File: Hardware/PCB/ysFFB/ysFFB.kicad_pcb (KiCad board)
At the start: 2 copper layers, 423.6 x 175 mm, 279 parts, among them J1 Synth_power_2x5, J10 AudioJack2, J11 AudioJack2, J12 AudioJack2, J13 AudioJack2, J14 AudioJack2, J15 Conn_01x04, J16 Conn_01x03, J2 Conn_01x08, J3 Conn_01x06, J4 Conn_01x04, J5 Conn_02x07_Odd_Even, J6 Conn_01x03, J7 Conn_01x08, J8 Conn_02x07_Odd_Even, J9 Conn_01x06, U1 TL074, U2 TL074, U3 TL074, U4 TL074, U5 TL074, U6 TL074, U7 TL074, U8 TL074

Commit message: Fix socket that looked suspiciously like a header. Fix every last remaining inconsistency.
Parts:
- J8: footprint Connector_PinHeader_2.54mm:PinHeader_2x07_P2.54mm_Vertical -> Connector_PinSocket_2.54mm:PinSocket_2x07_P2.54mm_Vertical
- moved J8 2.54 mm to (-28.8, 183.9)
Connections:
- J15 pad 2: ALL_P -> ODD_P
- J15 pad 3: ODD_P -> EVEN_P
- J15 pad 4: EVEN_P -> ALL_P
- J7 pad 1: /Panel components/BP8PP -> /Panel components/BP7PP
- J7 pad 2: /Panel components/BP6PP -> /Panel components/BP5PP
- J7 pad 3: /Panel components/BP4PP -> /Panel components/BP3PP
- J7 pad 4: /Panel components/BP2PP -> /Panel components/BP1PP
- J7 pad 5: /Panel components/BP1PP -> /Panel components/BP2PP
- J7 pad 6: /Panel components/BP3PP -> /Panel components/BP4PP
- J7 pad 7: /Panel components/BP5PP -> /Panel components/BP6PP
- J7 pad 8: /Panel components/BP7PP -> /Panel components/BP8PP
- J9 pad 1: /Panel components/HPPP -> /Panel components/LPP
- J9 pad 2: /Panel components/BP12P -> /Panel components/BP11PP
- J9 pad 3: /Panel components/BP10PP -> /Panel components/BP9PP
- J9 pad 4: /Panel components/BP9PP -> /Panel components/BP10PP
- J9 pad 5: /Panel components/BP11PP -> /Panel components/BP12P
- J9 pad 6: /Panel components/LPP -> /Panel components/HPPP
- RV1 pad 3: /Panel components/BP8PP -> /Panel components/BP7PP
- RV10 pad 3: /Panel components/BP12P -> /Panel components/BP11PP
- RV11 pad 3: /Panel components/BP10PP -> /Panel components/BP9PP
- RV12 pad 3: /Panel components/BP9PP -> /Panel components/BP10PP
- RV13 pad 3: /Panel components/BP11PP -> /Panel components/BP12P
- RV14 pad 3: /Panel components/LPP -> /Panel components/HPPP
- RV2 pad 3: /Panel components/BP6PP -> /Panel components/BP5PP
- RV3 pad 3: /Panel components/BP4PP -> /Panel components/BP3PP
- RV4 pad 3: /Panel components/BP2PP -> /Panel components/BP1PP
- RV5 pad 3: /Panel components/BP1PP -> /Panel components/BP2PP
- RV6 pad 3: /Panel components/BP3PP -> /Panel components/BP4PP
- RV7 pad 3: /Panel components/BP5PP -> /Panel components/BP6PP
- RV8 pad 3: /Panel components/BP7PP -> /Panel components/BP8PP
- RV9 pad 3: /Panel components/HPPP -> /Panel components/LPP
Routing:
- net /Panel components/LPP: track 111.0 -> 260.8 mm
- net /Panel components/HPPP: track 260.8 -> 111.0 mm
- net P2_12: track 235.1 -> 175.7 mm
- net P2_H: track 183.4 -> 242.6 mm
- net P2_11: track 154.3 -> 210.9 mm
- net P2_10: track 201.7 -> 146.6 mm
- net P2_8: track 171.8 -> 117.5 mm
- net P2_9: track 125.3 -> 179.3 mm
- net P2_7: track 96.2 -> 147.6 mm
- net P2_5: track 67.2 -> 115.9 mm
- net P2_3: track 38.1 -> 84.2 mm
- net P2_6: track 132.4 -> 88.5 mm
- net P2_4: track 100.6 -> 60.2 mm
- net P2_2: track 61.8 -> 30.8 mm
- net /Panel components/BP9PP: track 120.6 -> 134.7 mm
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
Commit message: submodules
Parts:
- removed G***: LOGO, ysFFB:ysFFB-aux-slide2_holes
- added GRAF1: Holes, ysFFB:ysFFB-aux-slide2_holes, F.Cu at (-104.2, 121.0)
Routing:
- net +12V: track 401.6 -> 402.8 mm

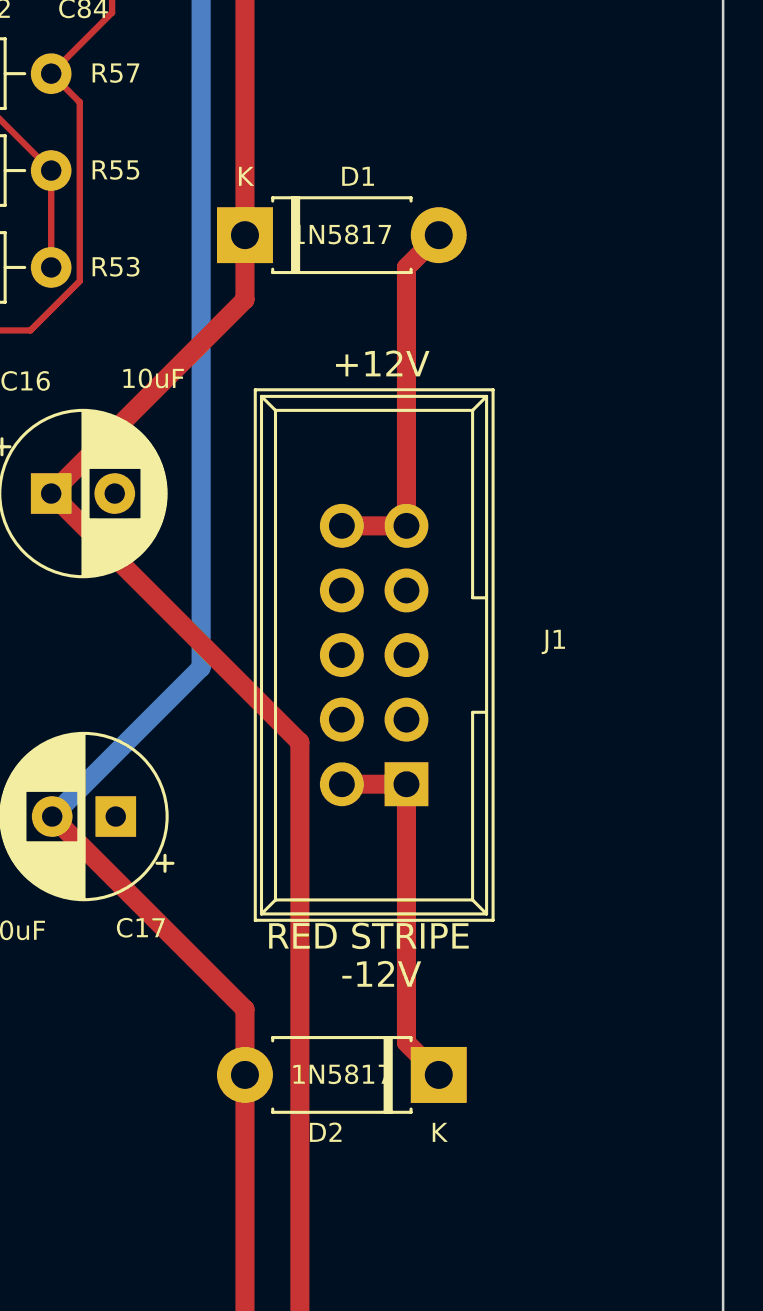
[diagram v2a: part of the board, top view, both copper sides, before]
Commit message: Clean up libraries, Schottky footprint update
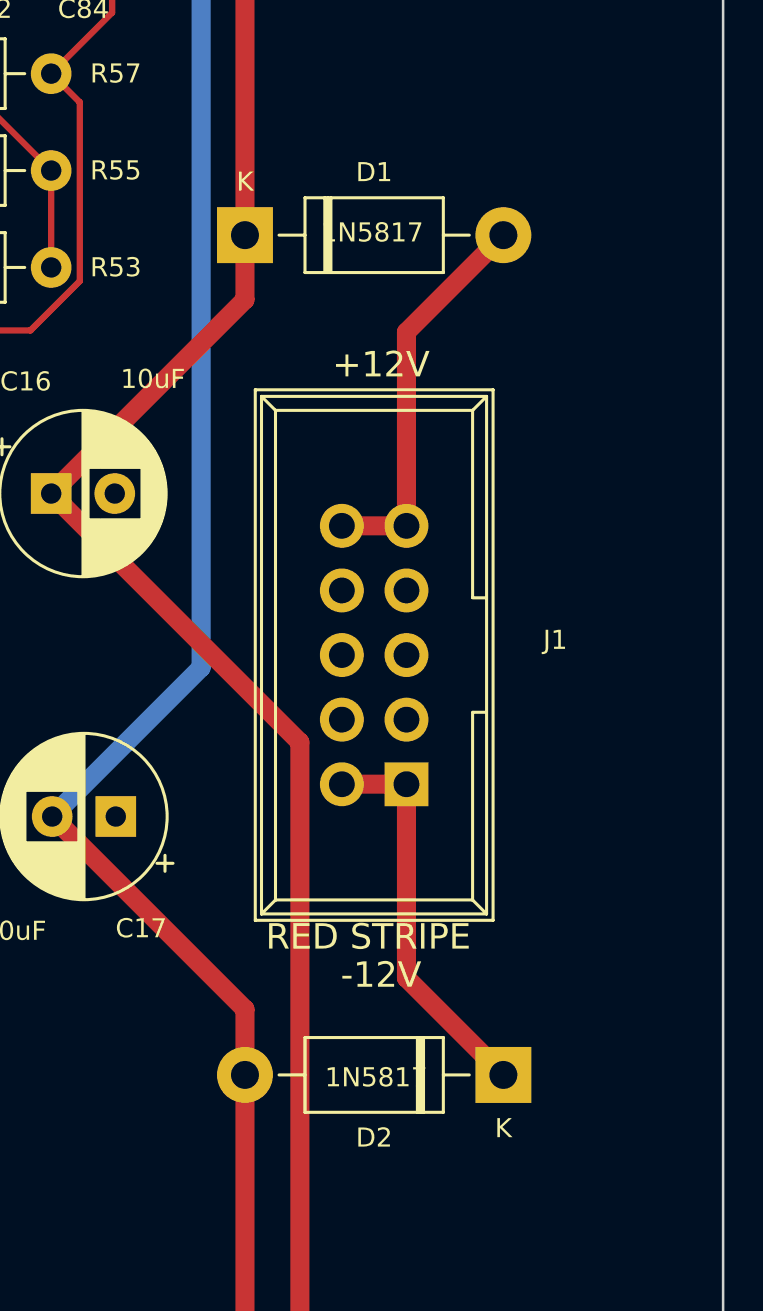
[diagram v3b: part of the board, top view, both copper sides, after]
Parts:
- D1, D2: footprint ao_tht:D_DO-41_SOD81_P7.62mm_Horizontal -> ao_tht:D_DO-41_SOD81_P10.16mm_Horizontal
- moved D2 2.54 mm to (213.8, 133.1)
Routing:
- net /+12_IN: track 14.5 -> 15.5 mm
- net /-12_IN: track 14.5 -> 15.5 mm

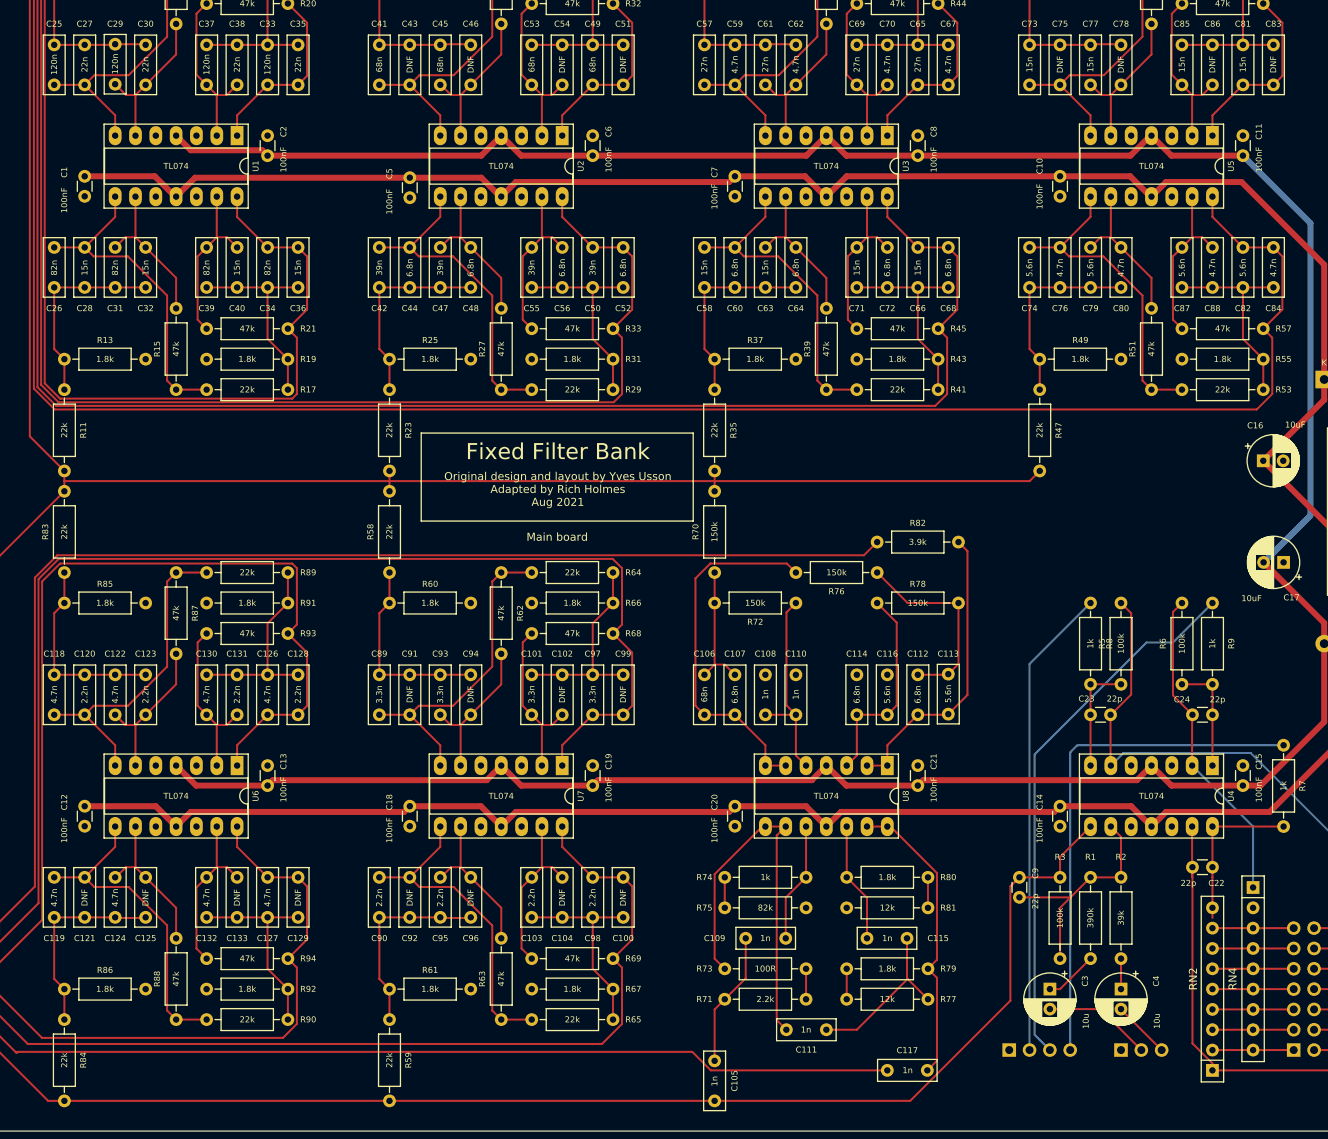
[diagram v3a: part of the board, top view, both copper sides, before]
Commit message: Cap vals on PCB, revised panel
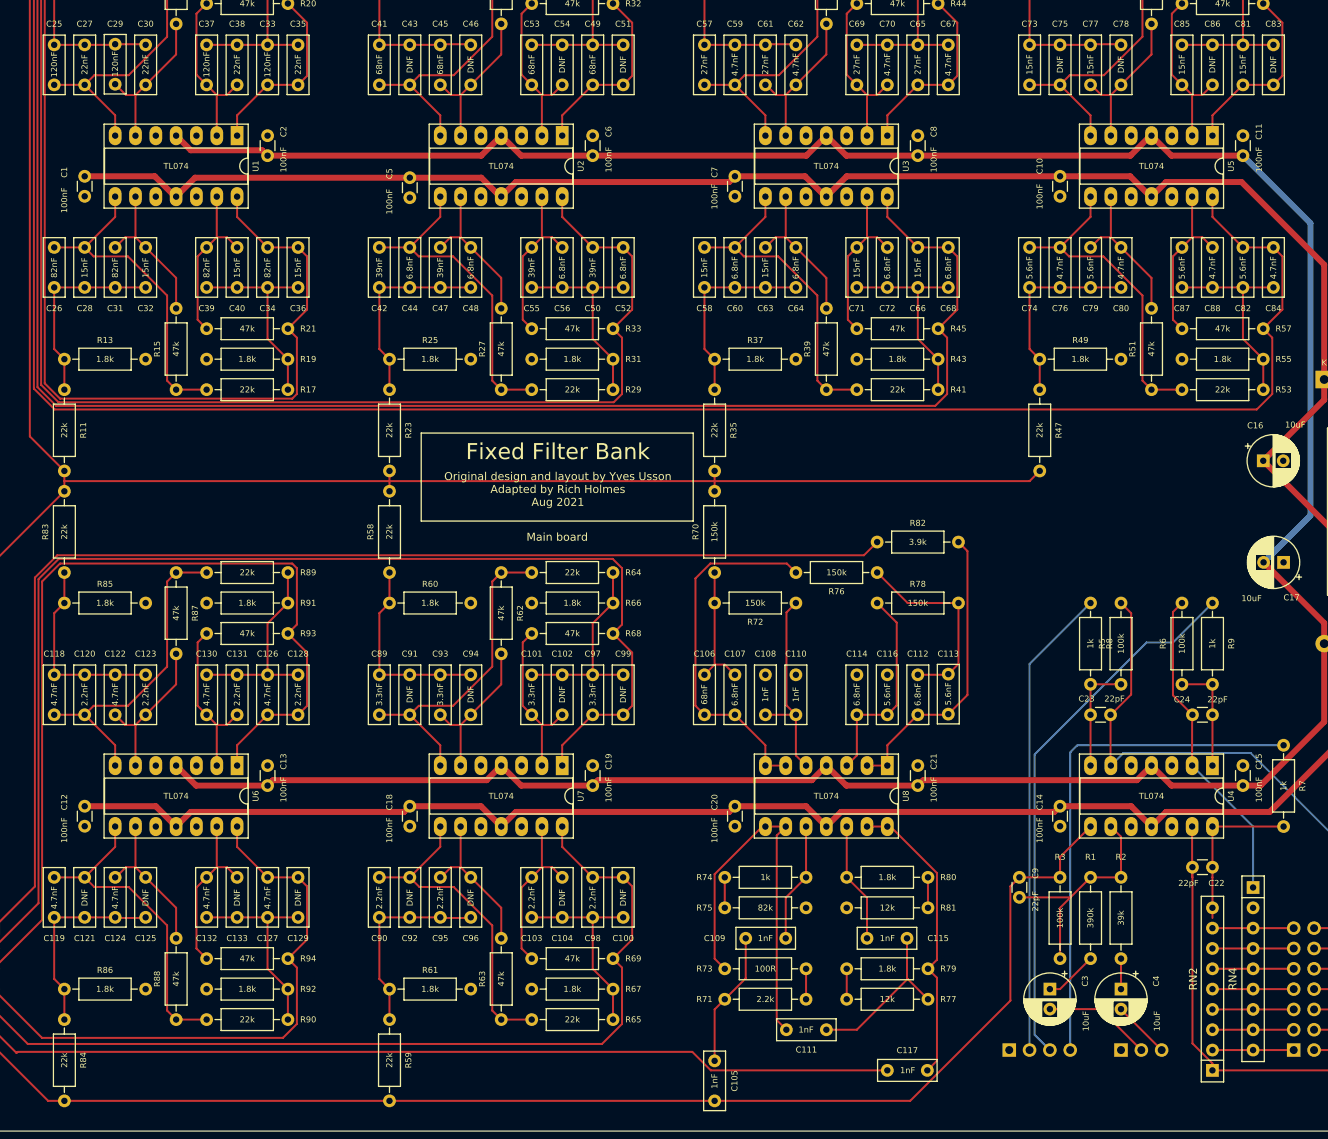
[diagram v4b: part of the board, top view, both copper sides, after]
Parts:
- C101, C89, C93, C97: value 3.3n -> 3.3nF
- C103, C120, C123, C128, C131, C90, C95, C98: value 2.2n -> 2.2nF
- C105, C108, C109, C110, C111, C115, C117: value 1n -> 1nF
- C106, C41, C45, C49, C53: value 68n -> 68nF
- C107, C112, C114, C44, C48, C52, C56, C60, C64, C68, C72: value 6.8n -> 6.8nF
- C113, C116, C74, C79, C82, C87: value 5.6n -> 5.6nF
- C118, C119, C122, C124, C126, C127, C130, C132, C59, C62, C67, C70, C76, C80, C84, C88: value 4.7n -> 4.7nF
- C22, C23, C24, C9: value 22p -> 22pF
- C25, C29, C33, C37: value 120n -> 120nF
- C26, C31, C34, C39: value 82n -> 82nF
- C27, C30, C35, C38: value 22n -> 22nF
- C28, C32, C36, C40, C58, C63, C66, C71, C73, C77, C81, C85: value 15n -> 15nF
- C3, C4: value 10u -> 10uF
- C42, C47, C50, C55: value 39n -> 39nF
- C57, C61, C65, C69: value 27n -> 27nF
